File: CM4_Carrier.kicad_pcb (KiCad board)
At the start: 4 copper layers, 47 x 88.8 mm, 99 parts, among them J1 Conn_01x22_Female, J10 Conn_01x20, J13 BM04B-GHS-TBT(LF)(SN)(N), J14 BM04B-GHS-TBT(LF)(SN)(N), J15 Conn_01x22_Female, J16 XT30, J17 Molex 470531000, J18 BM04B-GHS-TBT(LF)(SN)(N), J2 Conn_01x22_Female, J21 BM04B-GHS-TBT(LF)(SN)(N), J3 USB4085-GF-A_REVA, J7 Micro_SD_Card_Det, J8 HDMI_D_1.4, J9 Conn_02x08_Odd_Even, Q1 DMP3013SFV-7, SW1 SW_SPST, U1 TPD4EUSB30, U10 AP22653W6, U11 EMC2301-1-ACZL-TR, U12 RT9742SNGV, U13 FSUSB42MUX, U18 RT9742GGJ5, U2 TPD4EUSB30, U3 LMR33640DDDAR, U4 TPD4EUSB30, U6 USB2514B-I/M2, U7 AP22653W6, U9 74LVC1G07SE-7, Y1 ECS-240-18-33-JGN-TR

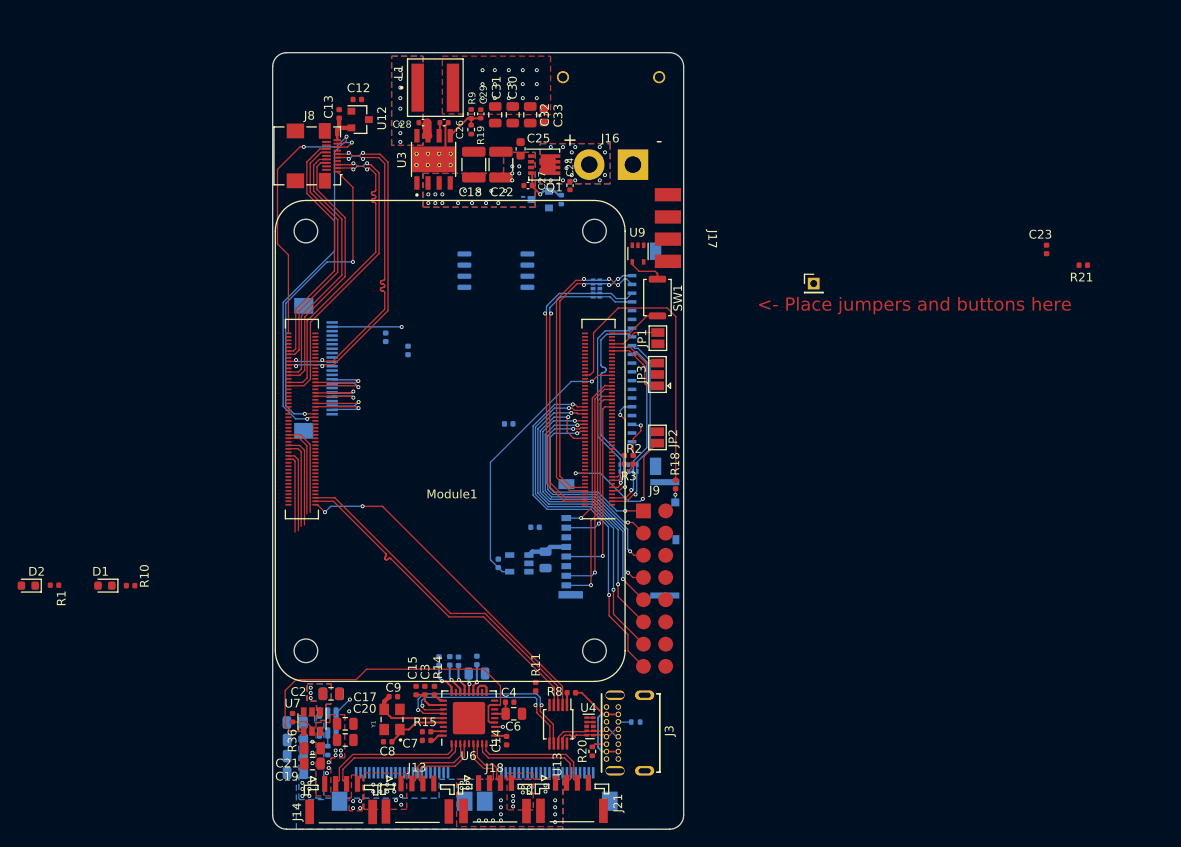
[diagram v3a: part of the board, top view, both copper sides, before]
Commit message: Changed footprint to match CM4, removed Ethernet and HDMI
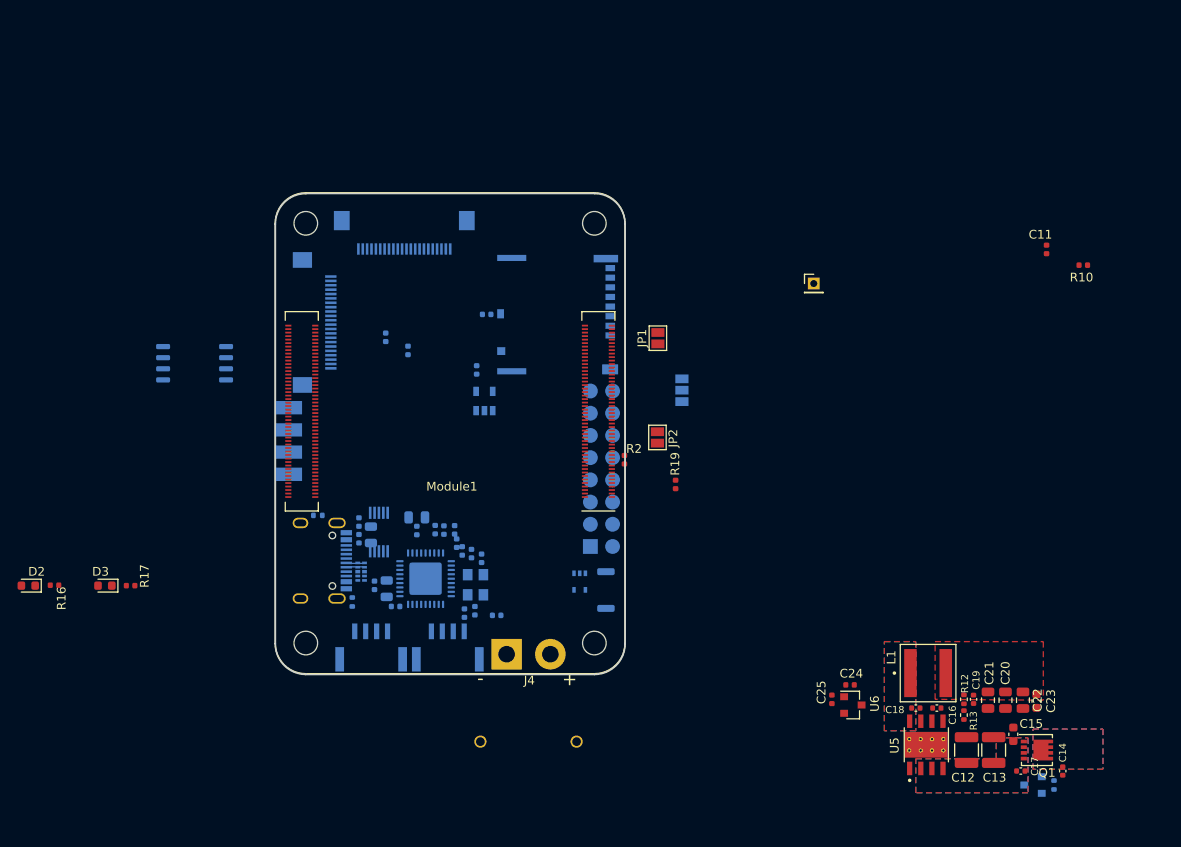
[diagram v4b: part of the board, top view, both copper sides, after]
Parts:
- removed the C1 at (140.2, 96.8)
- removed the C17 at (121.5, 131.2)
- removed the C19 at (117.8, 135.7)
- removed the C2 at (119.9, 127.7)
- removed the C20 at (121.5, 133.0)
- removed the C21 at (117.8, 133.9)
- removed C48, C53, C54, C55, C56: 10u, Capacitor_SMD:C_0805_2012Metric
- removed J10: Conn_01x20, Connector_FFC-FPC:Molex_200528-0200_1x20-1MP_P1.00mm_Horizontal
- removed J15: Conn_01x22_Female, Connector_FFC-FPC:Hirose_FH12-22S-0.5SH_1x22-1MP_P0.50mm_Horizontal
- removed J18, J21: BM04B-GHS-TBT(LF)(SN)(N), Connectors_JST:JST_GH_SM04B-GHS-TB_04x1.25mm_Angled
- removed the J3 at (155.4, 132.2)
- removed the J8 at (115.8, 66.2)
- removed the R3 at (154.4, 101.0)
- removed R31: 49.9k, Resistor_SMD:R_0402_1005Metric
- removed R36: 15K 1%, Resistor_SMD:R_0402_1005Metric
- removed the U1 at (153.9, 101.9)
- removed U10: AP22653W6, Package_TO_SOT_SMD:SOT-23-6
- removed the U2 at (150.2, 81.4)
- removed the U7 at (117.7, 130.9)
- added J1: USB_C_Receptacle, CM4IO:USB-C-SMD_TYPE-C-USB-17, B.Cu at (119.0, 112.5)
- C1: renamed from C8; moved to B.Cu
- C10: renamed from C4; moved to B.Cu
- C2: renamed from C9; moved to B.Cu
- C3: renamed from C6; moved to B.Cu
- C5: renamed from C7; moved to B.Cu
- C6: renamed from C3; moved to B.Cu
- C8: renamed from C14; moved to B.Cu
- C9: renamed from C15; moved to B.Cu
- J2: renamed from J13; moved to B.Cu
- J3: renamed from J14; moved to B.Cu
- J5: renamed from J17; moved to B.Cu
- J8: renamed from J9; moved to B.Cu
- JP3, SW1, Y1: moved to B.Cu
- R1: renamed from R11; moved to B.Cu
- R2: renamed from R8; moved to B.Cu
- R5: renamed from R14; moved to B.Cu
- R6: renamed from R15; moved to B.Cu
- R8: renamed from R20; moved to B.Cu
- U1: renamed from U13; moved to B.Cu
- U2: renamed from U6; moved to B.Cu
- U3: renamed from U4; moved to B.Cu
- U7: renamed from U9; moved to B.Cu
- moved C12 87.5 mm to (192.6, 134.2)
- moved C23 87.5 mm to (200.6, 128.6)
- moved R11 87.5 mm to (202.6, 138.2)
- moved C17 87.5 mm to (198.8, 136.6)
- moved U5 87.5 mm to (187.9, 133.6)
- moved U6 87.5 mm to (179.6, 129.0)
- moved C13 87.5 mm to (195.7, 134.2)
- moved C24 87.5 mm to (179.2, 126.7)
- moved D1 87.5 mm to (200.2, 138.2)
- moved Q1 87.5 mm to (200.6, 134.1)
- moved R13 87.5 mm to (192.2, 130.2)
- moved C14 87.5 mm to (203.5, 136.5)
- moved C15 87.5 mm to (197.9, 132.3)
- moved C16 87.5 mm to (189.2, 129.3)
- moved C18 87.5 mm to (186.8, 129.3)
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- renumbered C23 to C11, C18 to C12, C22 to C13, C24 to C14, C25 to C15, C26 to C16, C27 to C17, C28 to C18, C29 to C19, C30 to C20, C31 to C21, C32 to C22, C33 to C23, C12 to C24, C13 to C25, C5 to C26, C10 to C4, C11 to C7, D3 to D1, D1 to D3, J16 to J4, J1 to J6, J2 to J7, J7 to J9, R21 to R10, R4 to R11, R9 to R12, R19 to R13, R6 to R14, R7 to R15, R1 to R16, R10 to R17, R17 to R18, R18 to R19, R29 to R20, R12 to R3, R13 to R4, R16 to R7, R22 to R9, U11 to U4, U3 to U5, U12 to U6, U18 to U8
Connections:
- net /USB2-HUB/VBUS_HP renamed /USB2-HUB/+5V
- R2 pad 1: Net-(J10-Pad16) -> (no net)
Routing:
- net /CM4_GPIO ( Ethernet, GPIO, SDCARD)/GPIO2: track 42.7 -> 0.00 mm, vias 2 -> 0
- net /USBOTG: track 41.1 -> 0.00 mm, vias 2 -> 0
- net /CM4_HighSpeed/HDMI0_CEC: track 40.2 -> 0.00 mm, vias 2 -> 0
- net /CM4_GPIO ( Ethernet, GPIO, SDCARD)/GPIO3: track 39.5 -> 0.00 mm, vias 2 -> 0
- net /USB2-HUB/nOCS1: track 38.9 -> 0.00 mm
- net /USB2_P: track 38.9 -> 0.00 mm
- net /USB2_N: track 38.8 -> 0.00 mm
- net /CM4_HighSpeed/HDMI0_D0_N: track 37.8 -> 0.00 mm, vias 4 -> 0
- net /CM4_HighSpeed/HDMI0_D0_P: track 37.8 -> 0.00 mm, vias 4 -> 0
- net /CM4_GPIO ( Ethernet, GPIO, SDCARD)/TRD1_P: track 36.6 -> 0.00 mm, vias 1 -> 0
- net /CM4_GPIO ( Ethernet, GPIO, SDCARD)/GPIO4: track 36.2 -> 0.00 mm, vias 2 -> 0
- net /CM4_HighSpeed/HDMI0_HOTPLUG: track 36.2 -> 0.00 mm, vias 2 -> 0
- net /CM4_GPIO ( Ethernet, GPIO, SDCARD)/SD_DET: track 35.3 -> 0.00 mm
- net /CM4_HighSpeed/HDMI0_D2_N: track 35.3 -> 0.00 mm, vias 2 -> 0
- net /CM4_HighSpeed/HDMI0_D2_P: track 35.3 -> 0.00 mm, vias 2 -> 0
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- removed copper zone on B.Cu, net /+5v
- removed copper zone on F.Cu, net /USB2-HUB/+5V
- removed copper zone on In2.Cu, net /USB2-HUB/+5V
- removed copper zone on B.Cu, net /USB2-HUB/VBUS_LP
- removed copper zone on F.Cu, net /USB2-HUB/VBUS_LP
- removed copper zone on F.Cu, net GND
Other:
- board size 47 x 88.8 mm -> 40 x 55 mm
- board text removed: "<- Place jumpers and buttons here"

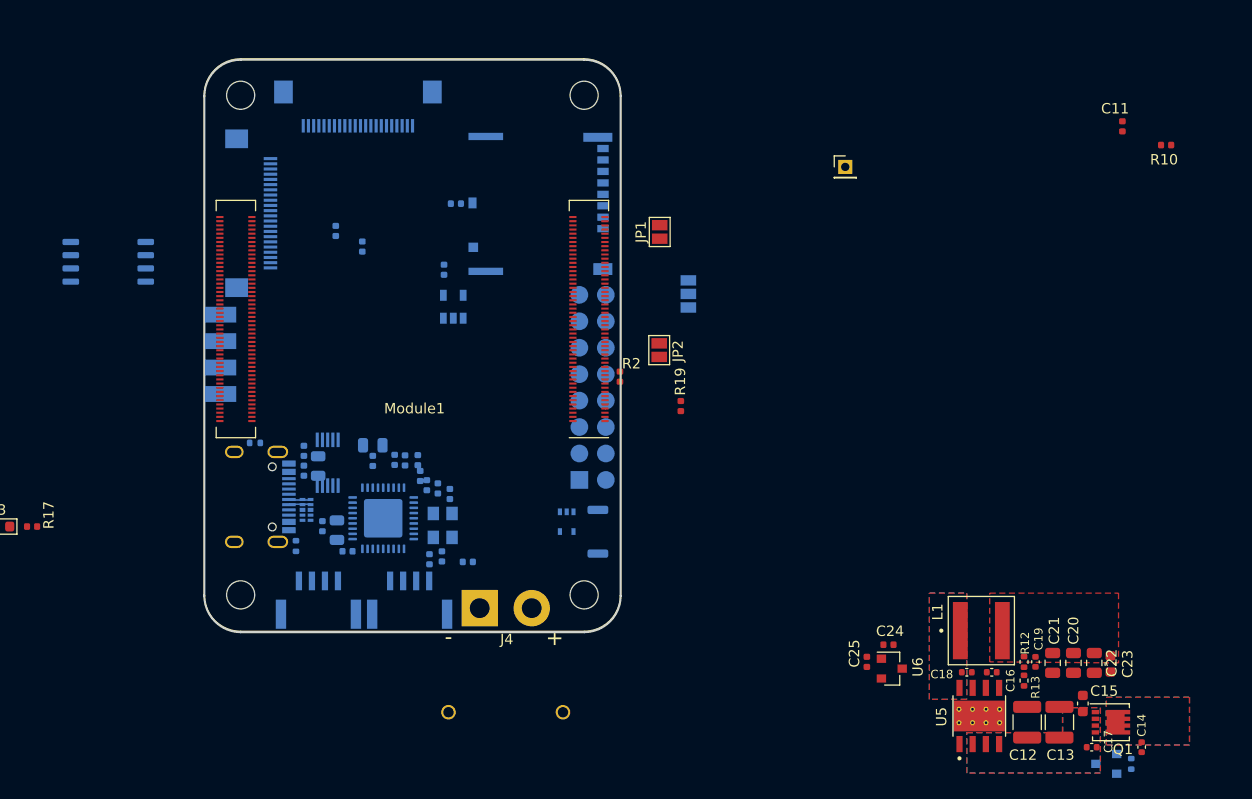
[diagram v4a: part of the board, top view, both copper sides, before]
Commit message: additional layout, power circuitry
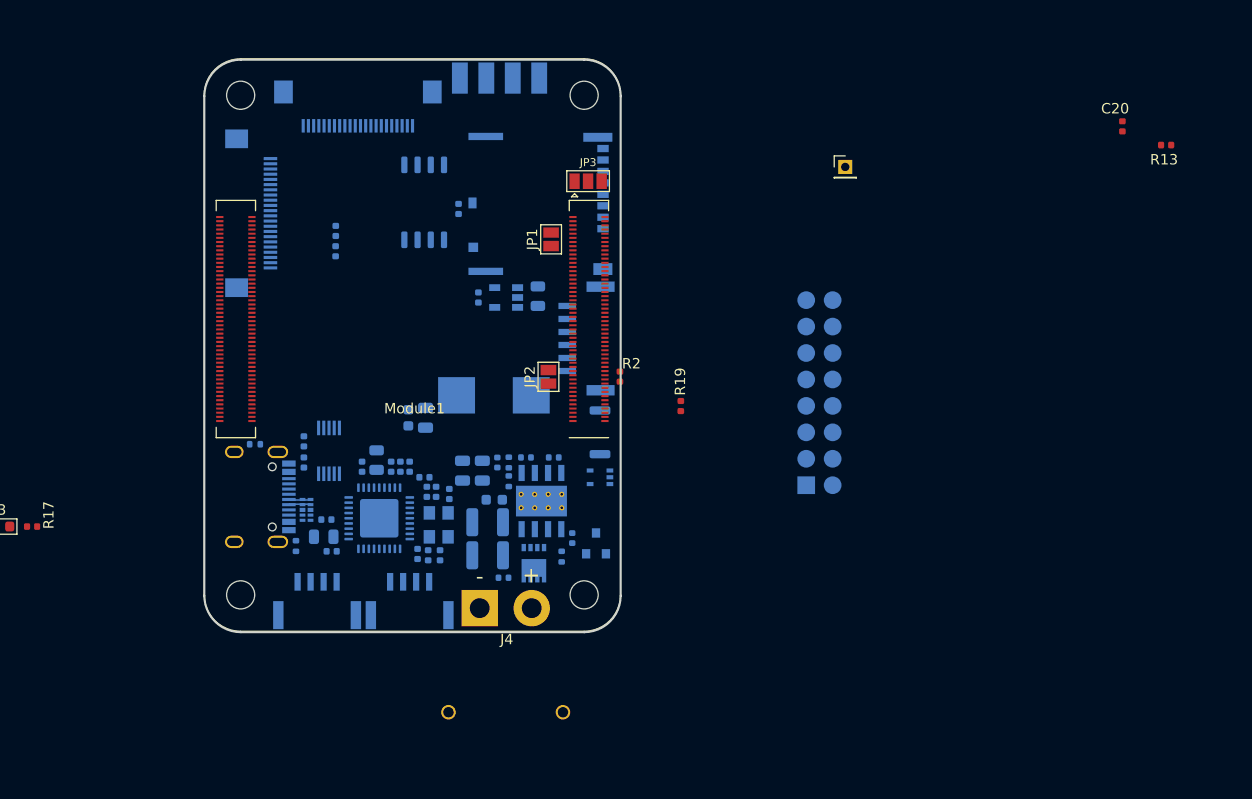
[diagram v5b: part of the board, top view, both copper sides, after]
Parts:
- removed the C24 at (179.2, 126.7)
- removed C25: 100n, Capacitor_SMD:C_0402_1005Metric
- removed the J2 at (124.5, 122.2)
- removed the U6 at (179.6, 129.0)
- added J1: SM04B-GHS-TB(LF)(SN)-, Open-HD:JST_SM04B-GHS-TB(LF)(SN)-, B.Cu at (124.3, 122.9)
- added J10: SM06B-GHS-TB(LF)(SN), Open-HD:JST_SM06B-GHS-TB(LF)(SN), B.Cu at (150.2, 97.3)
- C11: renamed from C12; moved to B.Cu
- C12: renamed from C14; moved to B.Cu
- C13, C21, C22, C23, Q1: moved to B.Cu
- C14: renamed from C15; moved to B.Cu
- C15: renamed from C16; moved to B.Cu
- C16: renamed from C17; moved to B.Cu
- C17: renamed from C18; moved to B.Cu
- C18: renamed from C19; moved to B.Cu
- C19: renamed from C20; moved to B.Cu
- J3: value BM04B-GHS-TBT(LF)(SN)(N) -> SM04B-GHS-TB(LF)(SN)-; footprint Connectors_JST:JST_GH_SM04B-GHS-TB_04x1.25mm_Angled -> Open-HD:JST_SM04B-GHS-TB(LF)(SN)-
- JP3: moved to F.Cu
- L1: footprint Open-HD:IND_XAL6060-472MEB -> CM4IO:HCM1A1105V2-4R7-R; moved to B.Cu
- R11: renamed from R12; moved to B.Cu
- R12: renamed from R13; moved to B.Cu
- U4: renamed from U5; moved to B.Cu
- moved C23 71.5 mm to (133.1, 104.9)
- moved C22 68.4 mm to (134.7, 104.9)
- moved C12 63.4 mm to (142.2, 120.3), turned to 180 degrees
- moved C19 61.5 mm to (138.3, 110.0)
- moved C14 59.8 mm to (141.4, 112.8), turned to 180 degrees
- moved R10 58.2 mm to (147.8, 118.2)
- moved C21 57.8 mm to (140.2, 110.0)
- moved Q1 57.5 mm to (145.2, 118.9), turned to -90 degrees
- moved C13 57.2 mm to (140.7, 118.1), turned to 180 degrees
- moved C11 55.3 mm to (140.7, 114.9), turned to 180 degrees
- moved C18 55.1 mm to (141.6, 109.2)
- moved C16 53.8 mm to (148.8, 116.5), turned to -90 degrees
- moved D1 53.4 mm to (151.1, 117.0), turned to 90 degrees
- moved R11 53.1 mm to (142.7, 109.2)
- moved R12 53.1 mm to (142.7, 111.0)
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- renumbered C11 to C20, C26 to C24, J1 to J2, R11 to R10, R10 to R13, U4 to U5, U7 to U6, U8 to U7
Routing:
- removed copper zone on F.Cu, net /+5v
- removed copper zone on B.Cu, net /Power/+12v
- removed copper zone on F.Cu, net /Power/+12v
- removed copper zone on In1.Cu, net /Power/+12v
- removed copper zone on In2.Cu, net /Power/+12v
- removed copper zone on B.Cu, net Net-(C12-Pad1)
- removed copper zone on F.Cu, net Net-(C12-Pad1)
- removed copper zone on In1.Cu, net Net-(C12-Pad1)
- removed copper zone on In2.Cu, net Net-(C12-Pad1)
- removed copper zone on B.Cu, net Net-(C17-Pad2)
- removed copper zone on F.Cu, net Net-(C17-Pad2)
- removed copper zone on In1.Cu, net Net-(C17-Pad2)
- removed copper zone on In2.Cu, net Net-(C17-Pad2)
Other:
- board text removed: "12v DC Input Tip +ve"

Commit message: May23 update
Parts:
- removed the R2 at (153.4, 101.0)
- R19: moved to B.Cu
- moved U5 47.2 mm to (179.2, 68.8)
- moved J5 26.3 mm to (169.0, 64.9), turned to 0 degrees
- moved R19 25.5 mm to (137.6, 90.4), turned to 90 degrees
- moved R14 20.8 mm to (145.0, 95.8), turned to 0 degrees
- moved R15 20.5 mm to (145.0, 96.8), turned to 0 degrees
- moved C20 7.87 mm to (194.0, 78.7)
- moved R13 7.87 mm to (198.2, 80.5)
- moved R8 3.81 mm to (118.5, 117.5), turned to 0 degrees
- moved D3 2.36 mm to (94.2, 113.0)
- moved C23 1.72 mm to (134.8, 105.2)
- moved C22 1.62 mm to (133.2, 105.2)
- moved C17 0.79 mm to (146.3, 108.7)
- moved C9 0.70 mm to (135.1, 112.2), turned to 0 degrees
- moved C6 0.70 mm to (135.1, 111.3), turned to 0 degrees
- moved C16 0.54 mm to (148.8, 117.0)
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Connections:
- U4 pad 10: (no net) -> GND
- U4 pad 11: (no net) -> GND
- U4 pad 12: (no net) -> GND
- U4 pad 13: (no net) -> GND
- U4 pad 14: (no net) -> GND
- U4 pad 15: (no net) -> GND
- U4 pad 16: (no net) -> GND
- U4 pad 17: (no net) -> GND
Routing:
- net /CM4_GPIO ( Ethernet, GPIO, SDCARD)/SD_DAT1: track 0.00 -> 15.8 mm, vias 0 -> 1
- net /CM4_GPIO ( Ethernet, GPIO, SDCARD)/SD_CLK: track 0.00 -> 13.7 mm, vias 0 -> 1
- net GND: track 0.00 -> 13.1 mm, vias 0 -> 12
- net /USB2-HUB/HD2_P: track 0.00 -> 9.40 mm
- net /USB2-HUB/HD2_N: track 0.00 -> 9.40 mm
- net /+3.3v: track 0.00 -> 7.78 mm
- net Net-(C16-Pad2): track 0.00 -> 6.86 mm
- net Net-(J2-PadA5): track 0.00 -> 5.91 mm
- net /Power/+12v: track 0.00 -> 5.75 mm, vias 0 -> 8
- net /CM4_GPIO ( Ethernet, GPIO, SDCARD)/SD_DAT2: track 0.00 -> 5.62 mm, vias 0 -> 1
- net Net-(C2-Pad1): track 0.00 -> 5.36 mm
- net /CM4_GPIO ( Ethernet, GPIO, SDCARD)/UART0_TX: track 0.00 -> 5.31 mm, vias 0 -> 1
- net Net-(J2-PadB5): track 0.00 -> 5.10 mm
- net /CM4_GPIO ( Ethernet, GPIO, SDCARD)/SD_DAT0: track 0.00 -> 4.57 mm, vias 0 -> 1
- net /USB2-HUB/USBD_N: track 2.16 -> 6.36 mm
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- added copper zone on B.Cu, net /+5v
- added copper zone on F.Cu, net /+5v
- added copper zone on In1.Cu, net /+5v
- added copper zone on B.Cu, net /Power/+12v
- added copper zone on F.Cu, net /Power/+12v
- added copper zone on In1.Cu, net /Power/+12v
- added copper zone on In2.Cu, net /Power/+12v
- added copper zone on B.Cu, net Net-(C12-Pad1)
- added copper zone on F.Cu, net Net-(C12-Pad1)
- added copper zone on In1.Cu, net Net-(C12-Pad1)
- added copper zone on In2.Cu, net Net-(C12-Pad1)
- added copper zone on B.Cu, net Net-(C17-Pad2)
- added copper zone on F.Cu, net Net-(C17-Pad2)
- added copper zone on In1.Cu, net Net-(C17-Pad2)
- removed copper zone on In1.Cu, net /+3.3v
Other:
- board text removed: "External USB"
- board text removed: "FAN"
